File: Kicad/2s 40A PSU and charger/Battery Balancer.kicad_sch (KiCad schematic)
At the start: 20 parts, among them Q6 Vishay sir404dp, or SiR500DP, U1 BQ76905RGRR

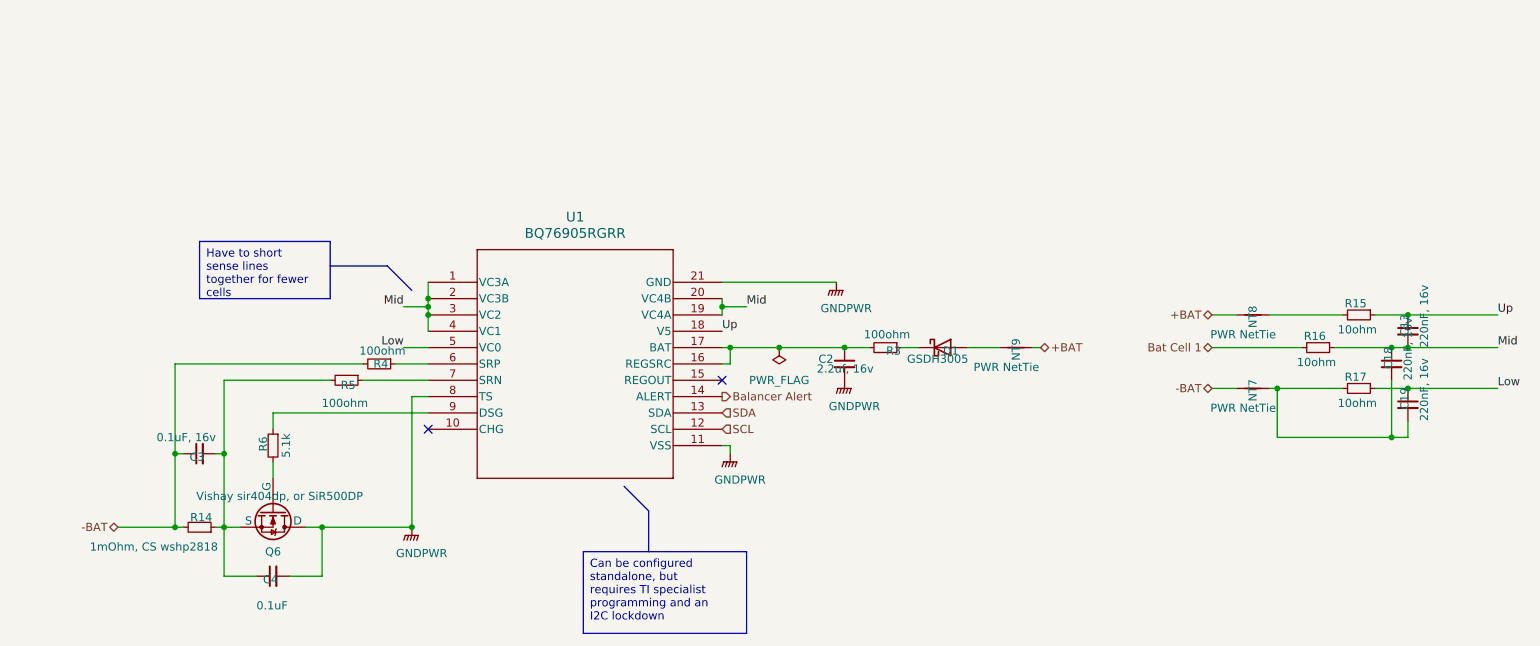
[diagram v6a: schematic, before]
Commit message: Changed default via sizes
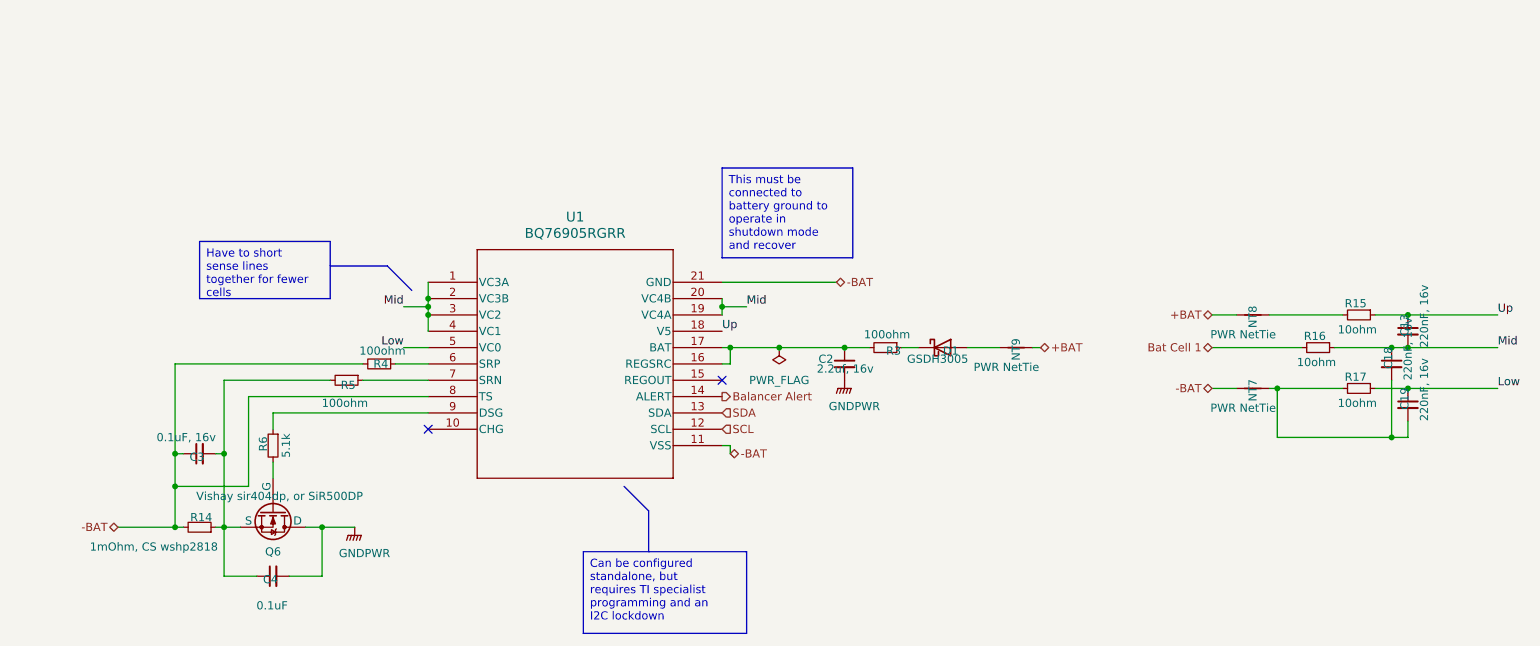
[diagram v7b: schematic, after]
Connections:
- net -BAT: now also U1.11 (VSS), U1.21 (GND), U1.8 (TS)
- net GNDPWR: no longer U1.11 (VSS), U1.21 (GND), U1.8 (TS)
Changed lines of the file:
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@@
+	)
+	(junction
+		(at 62.23 106.68)
+		(diameter 0)
+		(color 0 0 0 0)
 	)
 	(junction
@@
 	)
 	(junction
-		(at 99.06 113.03)
-		(diameter 0)
-		(color 0 0 0 0)
-	)
-	(junction
 		(at 254 91.44)
 		(diameter 0)
@@
 	(wire
 		(pts
-			(xy 99.06 92.71) (xy 101.6 92.71)
-		)
-		(stroke
-			(width 0)
-			(type default)
-		)
-	)
-	(wire
-		(pts
 			(xy 101.6 74.93) (xy 101.6 77.47)
 		)
@@
 	(wire
 		(pts
-			(xy 85.09 113.03) (xy 99.06 113.03)
+			(xy 85.09 113.03) (xy 90.17 113.03)
 		)
 		(stroke
@@
 	(wire
 		(pts
+			(xy 73.66 106.68) (xy 62.23 106.68)
+		)
+		(stroke
+			(width 0)
+			(type default)
+		)
+	)
+	(wire
+		(pts
+			(xy 73.66 92.71) (xy 73.66 106.68)
+		)
+		(stroke
+			(width 0)
+			(type default)
+		)
+	)
+	(wire
+		(pts
 			(xy 148.59 85.09) (xy 156.21 85.09)
 		)
@@
 	(wire
 		(pts
-			(xy 99.06 92.71) (xy 99.06 113.03)
-		)
-		(stroke
-			(width 0)
-			(type default)
-		)
-	)
-	(wire
-		(pts
 			(xy 148.59 87.63) (xy 148.59 85.09)
 		)
@@
 	(wire
 		(pts
+			(xy 62.23 106.68) (xy 62.23 113.03)
+		)
+		(stroke
+			(width 0)
+			(type default)
+		)
+	)
+	(wire
+		(pts
 			(xy 147.32 100.33) (xy 148.59 100.33)
 		)
@@
 		)
 	)
+	(wire
+		(pts
+			(xy 73.66 92.71) (xy 101.6 92.71)
+		)
+		(stroke
+			(width 0)
+			(type default)
+		)
+	)
 	(polyline
 		(pts
@@
 	(wire
 		(pts
-			(xy 62.23 101.6) (xy 62.23 113.03)
+			(xy 62.23 101.6) (xy 62.23 106.68)
 		)
 		(stroke
@@
 			(width 0)
 			(type default)
+		)
+	)
+	(text_box "This must be connected to battery ground to operate in shutdown mode and recover"
+		(exclude_from_sim no)
+		(at 147.32 57.15 0)
+		(size 20.32 13.97)
+		(stroke
+			(width 0)
+			(type default)
+		)
+		(fill
+			(type none)
+		)
+		(effects
+			(font
+				(size 1.27 1.27)
+			)
+			(justify left top)
 		)
 	)
@@
 	(hierarchical_label "-BAT"
 		(shape bidirectional)
+		(at 148.59 101.6 0)
+		(fields_autoplaced yes)
+		(effects
+			(font
+				(size 1.27 1.27)
+			)
+			(justify left)
+		)
+		(property "Netclass" "High Current"
+			(at 148.59 102.87 0)
+			(effects
+				(font
+					(size 1.27 1.27)
+					(italic yes)
+				)
+				(justify left)
+			)
+		)
+	)
+	(hierarchical_label "-BAT"
+		(shape bidirectional)
 		(at 223.52 91.44 180)
 		(fields_autoplaced yes)
@@
 				)
 				(justify right)
+			)
+		)
+	)
+	(hierarchical_label "-BAT"
+		(shape bidirectional)
+		(at 165.1 74.93 0)
+		(fields_autoplaced yes)
+		(effects
+			(font
+				(size 1.27 1.27)
+			)
+			(justify left)
+		)
+		(property "Netclass" "High Current"
+			(at 165.1 76.2 0)
+			(effects
+				(font
+					(size 1.27 1.27)
+					(italic yes)
+				)
+				(justify left)
 			)
 		)
@@
 	)
 	(symbol
-		(lib_id "power:GNDPWR")
-		(at 148.59 101.6 0)
-		(unit 1)
-		(exclude_from_sim no)
-		(in_bom yes)
-		(on_board yes)
-		(dnp no)
-		(property "Reference" "#PWR02"
-			(at 148.59 106.68 0)
-			(effects
-				(font
-					(size 1.27 1.27)
-				)
-				(hide yes)
-			)
-		)
-		(property "Value" "GNDPWR"
-			(at 150.114 105.664 0)
-			(effects
-				(font
-					(size 1.27 1.27)
-				)
-			)
-		)
-		(property "Footprint" ""
-			(at 148.59 102.87 0)
-			(effects
-				(font
-					(size 1.27 1.27)
-				)
-				(hide yes)
-			)
-		)
-		(property "Datasheet" ""
-			(at 148.59 102.87 0)
-			(effects
-				(font
-					(size 1.27 1.27)
-				)
-				(hide yes)
-			)
-		)
-		(property "Description" "Power symbol creates a global label with name \"GNDPWR\" , global ground"
-			(at 148.59 101.6 0)
-			(effects
-				(font
-					(size 1.27 1.27)
-				)
-				(hide yes)
-			)
-		)
-		(pin "1"
-		)
-		(instances
-			(project "2s 40A PSU and charger"
-				(path "/eb3f183d-8bb1-43a5-a363-092ed67891e3/9cf42ac0-c980-41ef-957c-e7b7cc3eb205"
-					(reference "#PWR02")
-					(unit 1)
-				)
-			)
-		)
-	)
-	(symbol
 		(lib_id "BQ76905:BQ76905RGRR")
 		(at 101.6 74.93 0)
@@
 				(path "/eb3f183d-8bb1-43a5-a363-092ed67891e3/9cf42ac0-c980-41ef-957c-e7b7cc3eb205"
 					(reference "U1")
-					(unit 1)
-				)
-			)
-		)
-	)
-	(symbol
-		(lib_id "power:GNDPWR")
-		(at 165.1 74.93 0)
-		(unit 1)
-		(exclude_from_sim no)
-		(in_bom yes)
-		(on_board yes)
-		(dnp no)
-		(property "Reference" "#PWR04"
-			(at 165.1 80.01 0)
-			(effects
-				(font
-					(size 1.27 1.27)
-				)
-				(hide yes)
-			)
-		)
-		(property "Value" "GNDPWR"
-			(at 166.624 78.994 0)
-			(effects
-				(font
-					(size 1.27 1.27)
-				)
-			)
-		)
-		(property "Footprint" ""
-			(at 165.1 76.2 0)
-			(effects
-				(font
-					(size 1.27 1.27)
-				)
-				(hide yes)
-			)
-		)
-		(property "Datasheet" ""
-			(at 165.1 76.2 0)
-			(effects
-				(font
-					(size 1.27 1.27)
-				)
-				(hide yes)
-			)
-		)
-		(property "Description" "Power symbol creates a global label with name \"GNDPWR\" , global ground"
-			(at 165.1 74.93 0)
-			(effects
-				(font
-					(size 1.27 1.27)
-				)
-				(hide yes)
-			)
-		)
-		(pin "1"
-		)
-		(instances
-			(project "2s 40A PSU and charger"
-				(path "/eb3f183d-8bb1-43a5-a363-092ed67891e3/9cf42ac0-c980-41ef-957c-e7b7cc3eb205"
-					(reference "#PWR04")
 					(unit 1)
 				)
@@
 	(symbol
 		(lib_id "power:GNDPWR")
-		(at 99.06 113.03 0)
+		(at 90.17 113.03 0)
 		(unit 1)
 		(exclude_from_sim no)
@@
 		(dnp no)
 		(property "Reference" "#PWR01"
-			(at 99.06 118.11 0)
+			(at 90.17 118.11 0)
 			(effects
 				(font
@@
 		)
 		(property "Value" "GNDPWR"
-			(at 100.584 117.094 0)
+			(at 91.694 117.094 0)
 			(effects
 				(font
@@
 		)
 		(property "Footprint" ""
-			(at 99.06 114.3 0)
+			(at 90.17 114.3 0)
 			(effects
 				(font
@@
 		)
 		(property "Datasheet" ""
-			(at 99.06 114.3 0)
+			(at 90.17 114.3 0)
 			(effects
 				(font
@@
 		)
 		(property "Description" "Power symbol creates a global label with name \"GNDPWR\" , global ground"
-			(at 99.06 113.03 0)
-			(effects
-				(font
+			(at 90.17 113.03 0)
+			(effects
+				(font
